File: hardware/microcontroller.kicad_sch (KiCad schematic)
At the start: 12 parts, among them J3 AVR-ISP-6, SW2 SKRPACE010, U5 ATMEGA328P-AU, Y1 Crystal-32kHz

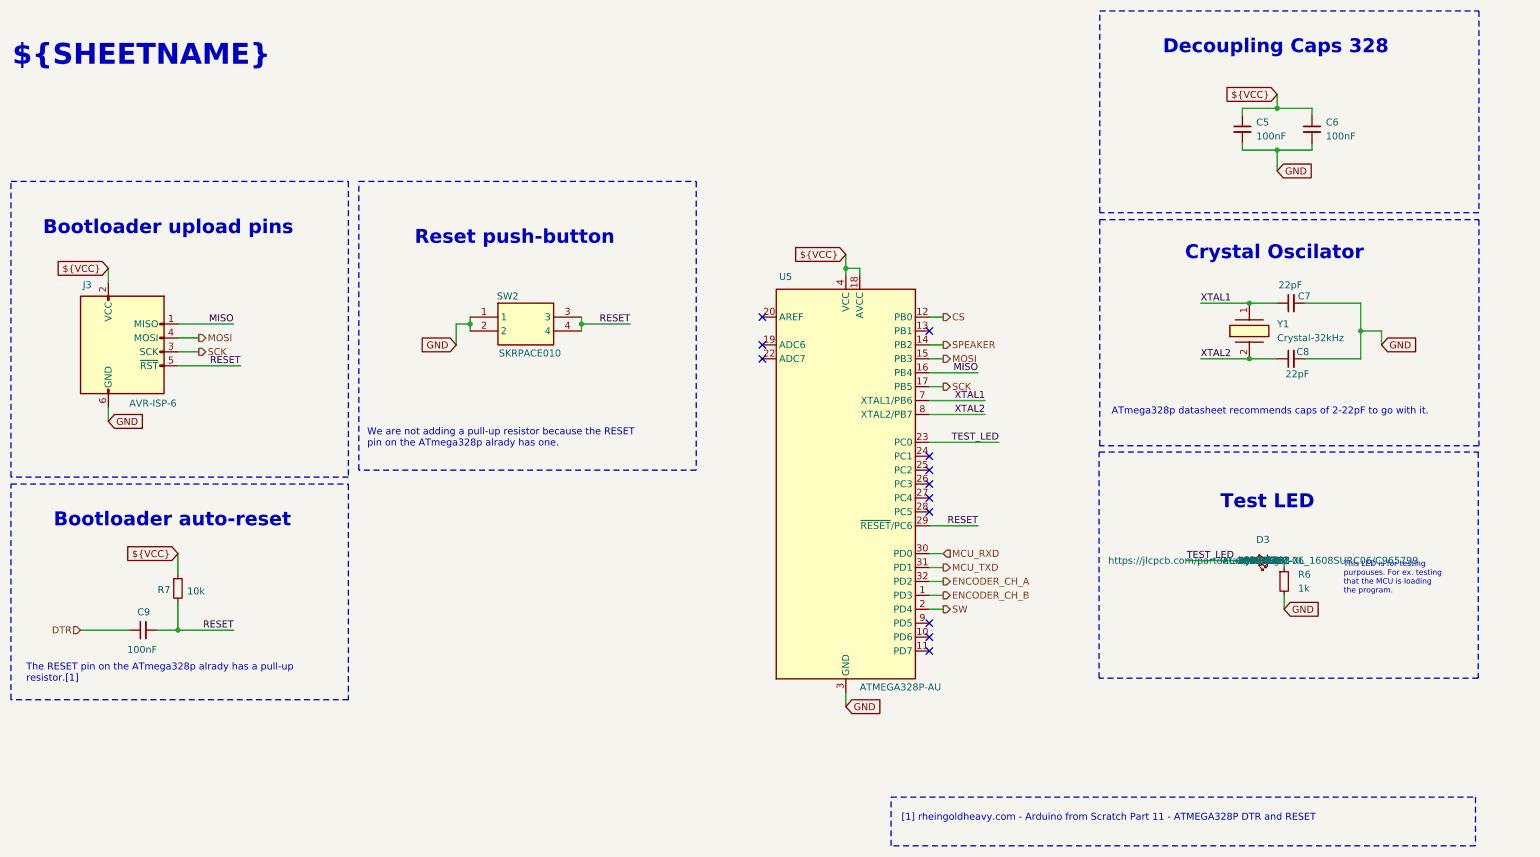
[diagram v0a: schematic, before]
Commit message: Added a pull up resistor to the CS line on the SPI and added two more test LEDs
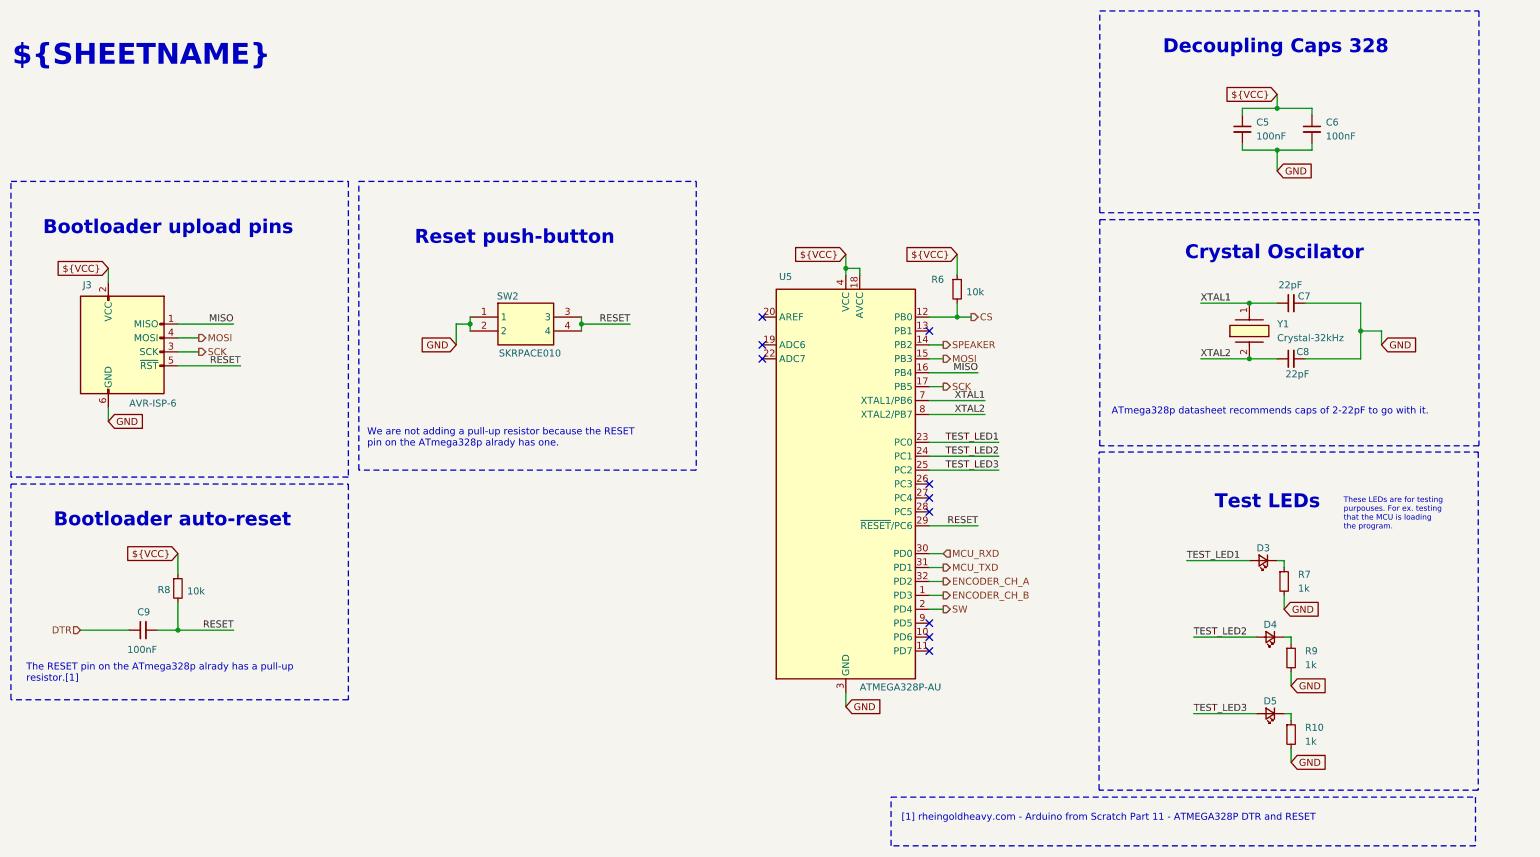
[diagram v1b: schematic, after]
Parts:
- added D4, D5: Red test LED, LED_SMD:LED_0603_1608Metric_Pad1.05x0.95mm_HandSolder, symbol Device:LED_Small
- added R10, R9: 1k, Resistor_SMD:R_0805_2012Metric_Pad1.20x1.40mm_HandSolder, symbol Device:R_Small
- added R6: 10k, Resistor_SMD:R_0805_2012Metric_Pad1.20x1.40mm_HandSolder, symbol Device:R_Small
- renumbered R6 to R7, R7 to R8
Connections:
- net ${VCC}: now also R6.1
- net CS: now also R6.2
- net GND: now also R10.2, R9.2
- net TEST_LED2: now reaches U5.24 (PC1)
- net TEST_LED2: now also D4.2 (A)
- net TEST_LED3: now reaches U5.25 (PC2)
- net TEST_LED3: now also D5.2 (A)
- net TEST_LED renamed TEST_LED1
- new net: D5.1 (K), R10.1
- new net: D4.1 (K), R9.1
- no-connect marks 12 -> 10
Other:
- note added: "Test LEDs"
- note removed: "Test LED"

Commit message: Changed the footprint of the crystal for one were the crystal is horizontal.
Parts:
- Y1: footprint kitchen_timer:FL26T2-32.000 -> Crystal:Crystal_C26-LF_D2.1mm_L6.5mm_Horizontal
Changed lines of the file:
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@@
 			)
 		)
-		(property "Footprint" "kitchen_timer:FL26T2-32.000"
+		(property "Footprint" "Crystal:Crystal_C26-LF_D2.1mm_L6.5mm_Horizontal"
 			(at 338.76 67.31 0)
 			(effects
@@
 			(at 242.57 76.2 0)
 			(effects
-				(font
-					(size 1.27 1.27)
-				)
-				(hide yes)
-			)
-		)
-		(property "Manufacturer_Name" ""
-			(at 242.57 76.2 0)
-			(effects
-				(font
-					(size 1.27 1.27)
-				)
-				(hide yes)
-			)
-		)
-		(property "Manufacturer_Part_Number" ""
-			(at 242.57 76.2 0)
-			(effects
-				(font
-					(size 1.27 1.27)
-				)
-				(hide yes)
-			)
-		)
-		(property "Mouser Part Number" ""
-			(at 242.57 76.2 0)
-			(effects
-				(font
-					(size 1.27 1.27)
-				)
-				(hide yes)
-			)
-		)
-		(property "Mouser Price/Stock" ""
-			(at 242.57 76.2 0)
-			(effects

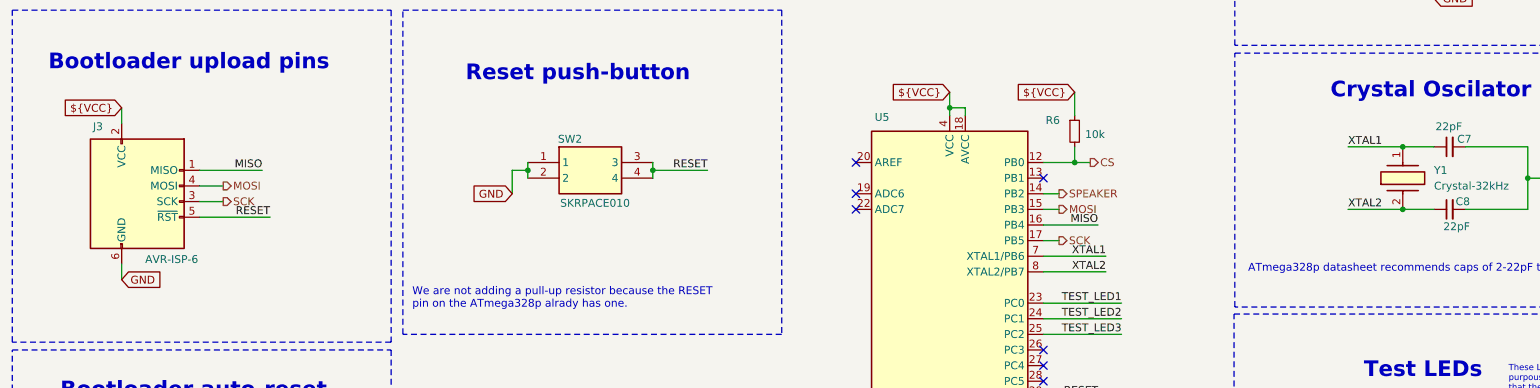
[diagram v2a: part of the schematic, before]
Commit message: Reviewed the Fields Table and marked all components that should not be populated. Then I runned rules check in the schematic and PCB
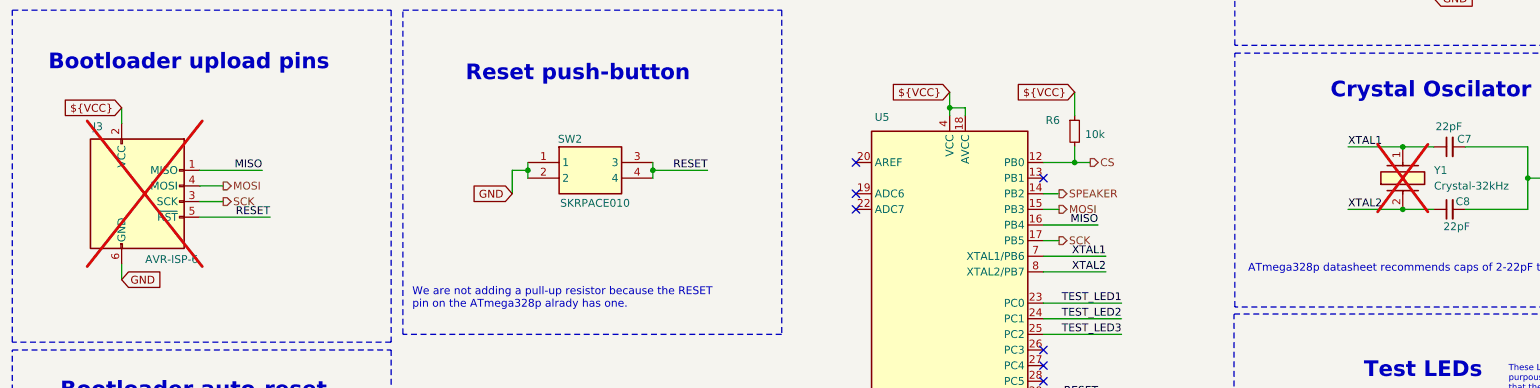
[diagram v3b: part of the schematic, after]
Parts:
- J3, Y1: now not fitted
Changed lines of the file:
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@@
 		(in_bom no)
 		(on_board yes)
-		(dnp no)
+		(dnp yes)
 		(fields_autoplaced yes)
 		(property "Reference" "Y1"
@@
 		(in_bom no)
 		(on_board yes)
-		(dnp no)
+		(dnp yes)
 		(property "Reference" "J3"
 			(at 31.242 62.738 0)

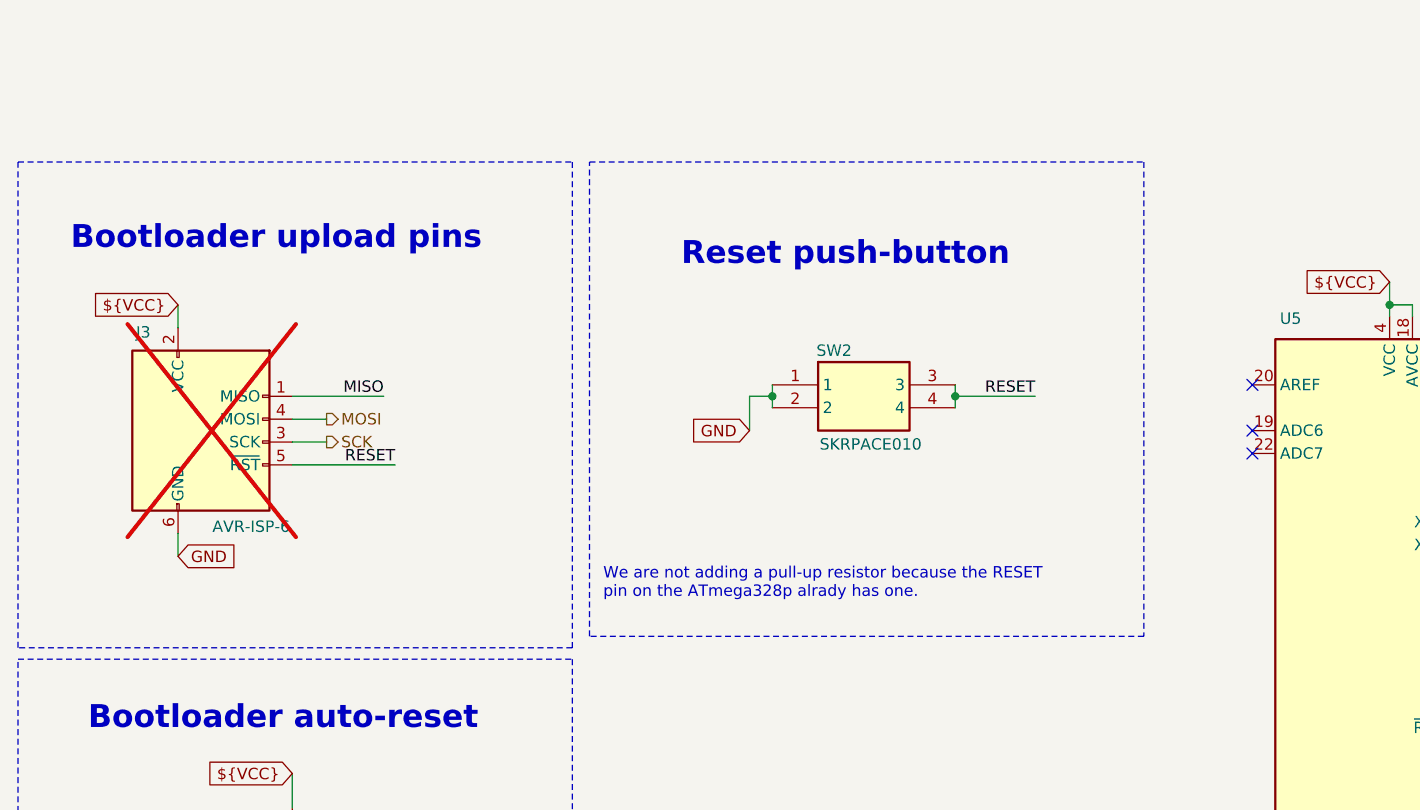
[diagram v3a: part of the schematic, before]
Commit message: Added Tx resistor, voltage devider for battery voltage mesurement.
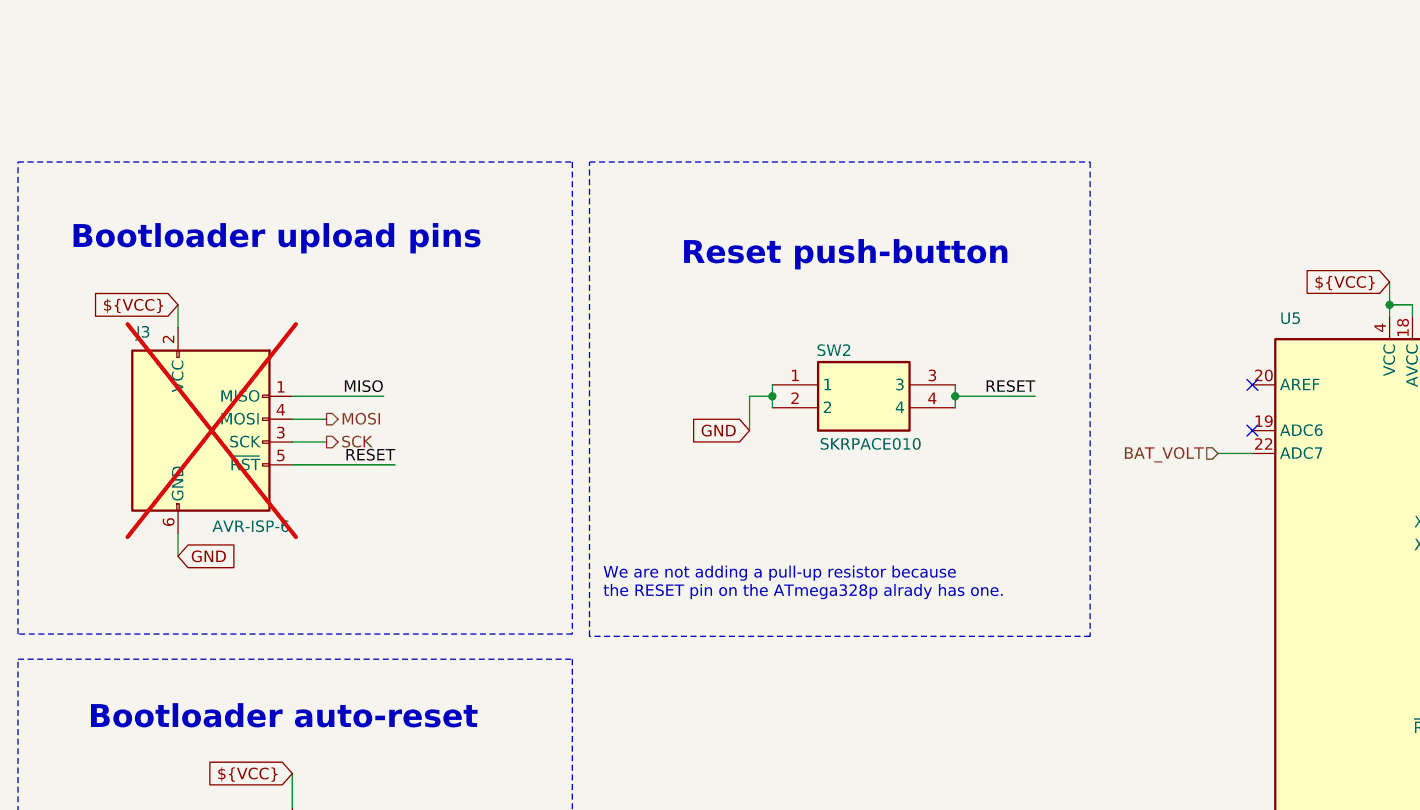
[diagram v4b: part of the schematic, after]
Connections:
- net BAT_VOLT: now reaches U5.22 (ADC7)
- no-connect marks 10 -> 9
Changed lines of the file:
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@@
 	(rectangle
 		(start 80.01 43.815)
-		(end 141.605 96.52)
+		(end 135.636 96.52)
 		(stroke
 			(width 0)
@@
 	(rectangle
 		(start 16.51 43.815)
-		(end 78.105 97.79)
+		(end 78.105 96.266)
 		(stroke
 			(width 0)
@@
 		)
 	)
-	(text "We are not adding a pull-up resistor because the RESET\npin on the ATmega328p alrady has one."
+	(text "We are not adding a pull-up resistor because\nthe RESET pin on the ATmega328p alrady has one."
 		(exclude_from_sim no)
 		(at 81.534 88.9 0)
@@
 	)
 	(no_connect
-		(at 153.67 76.2)
-	)
-	(no_connect
 		(at 184.15 127)
 	)
@@
 		(pts
 			(xy 171.45 60.96) (xy 171.45 59.69)
+		)
+		(stroke
+			(width 0)
+			(type default)
+		)
+	)
+	(wire
+		(pts
+			(xy 149.86 76.2) (xy 153.67 76.2)
 		)
 		(stroke
@@
 		)
 	)
+	(hierarchical_label "BAT_VOLT"
+		(shape input)
+		(at 149.86 76.2 180)
+		(effects
+			(font
+				(size 1.27 1.27)
+			)
+			(justify right)
+		)
+	)
